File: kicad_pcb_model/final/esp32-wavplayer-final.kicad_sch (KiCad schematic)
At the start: 0 parts

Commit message: Creating schematic
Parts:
- added C1, C3, UC13: 100nF, symbol Device:C
- added C10: C_Polarized_Small_US, Package_SO:SOIC-8_3.9x4.9mm_P1.27mm, symbol Device:C_Polarized_Small_US
- added C11, C7, C8, C9: C, symbol Device:C
- added C2: 10nF, symbol Device:C
- added C4, UC1, UC2, UC3: 1uF, symbol Device:C
- added C5, PC2: 10uF, symbol Device:C
- added C6: C, Display:OLED-128O064D, symbol Device:C
- added DB1: MicroSDDebug, symbol Connector:Conn_01x06_Pin
- added DB2: DisplayDebug, symbol Connector:Conn_01x04_Pin
- added DS1: Wisevision X096-2864KSWPG01-H30, Display:OLED-128O064D, symbol Display_Graphic:OLED-128O064D
- added MSD1: Generic MicroSD, Module:Maple_Mini, symbol Connector:Micro_SD_Card_Det1
- added PC1: 10uF, Package_TO_SOT_SMD:SOT-23-5, symbol Device:C
- added R1, R2, R3, R4: 10k, symbol Device:R
- added R10, R7, R8, R9: 22R, symbol Device:R
- added R11: R, symbol Device:R
- added R5, R6: 5.1K, Package_DIP:DIP-8_W7.62mm, symbol Device:R
- added U1: ESP32-C3, Package_DFN_QFN:QFN-32-1EP_5x5mm_P0.5mm_EP3.45x3.45mm, symbol PCM_Espressif:ESP32-C3
- added U2: ME6211C33M5, Package_TO_SOT_SMD:SOT-23-5, symbol Regulator_Linear:ME6211C33M5
- added USB1: USBC-6Pin, symbol Connector:USB_C_Receptacle_USB2.0_14P
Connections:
- new net: C11.2, DS1.28 (VCC)
- new net: R6.1, USB1.A5 (CC1)
- new net: R10.2, USB1.A6 (D+)
- new net: R7.2, USB1.A7 (D-)
- new net: R5.1, USB1.B5 (CC2)
- new net: R9.2, USB1.B6 (D+)
- new net: R8.2, USB1.B7 (D-)
- new net: DS1.26 (IREF), R11.2
- new net: C8.1, DS1.6 (VBAT)
- new net: C9.1, DS1.12 (BS2), DS1.9 (VDD)
- new net: C6.2, DS1.2 (C2N)
- new net: C10.1, DS1.27 (VCOMH)
- new net: C6.1, DS1.3 (C2P)
- new net: C7.1, DS1.4 (C1P)
- new net: C7.2, DS1.5 (C1N)
- new net +3V3: C1.1, C2.1, C3.1, C4.1, C5.1, DB1.1 (Pin_1), MSD1.4 (VDD), PC2.1, R1.1, R2.1, R3.1, R4.1, U1.11 (VDD3P3_RTC), U1.17 (VDD3P3_CPU), U1.2 (VDD3P3), U1.3 (VDD3P3), U1.31 (VDDA), U1.32 (VDDA), U2.5 (V_{OUT}), UC1.1, UC13.2, UC2.1, UC3.1
- new net Earth: C1.2, C10.2, C11.1, C2.2, C3.2, C4.2, C5.2, C8.2, C9.2, DB1.6 (Pin_6), DS1.1 (GND), DS1.10 (BS0), DS1.11 (BS1), DS1.29 (VLSS), DS1.30 (GND), DS1.8 (VSS), MSD1.6 (VSS), PC1.2, PC2.2, R11.1, R5.2, R6.2, U1.33 (GND), U2.2 (V_{SS}), UC1.2, UC13.1, UC2.2, UC3.2, USB1.A1 (GND), USB1.A12 (GND), USB1.B1 (GND), USB1.B12 (GND)
- new net GPIO18/USB_D+: R10.1, R9.1
- new net GPIO18/USB_D-: U1.25 (GPIO18/USB_D-)
- new net GPIO19/USB_D+: U1.26 (GPIO19/USB_D+)
- new net GPIO19/USB_D-: R7.1, R8.1
- new net GPIO4: DB1.4 (Pin_4), MSD1.5 (CLK), R2.2, U1.9 (MTMS/GPIO4/ADC1_CH4)
- new net GPIO5: DB1.5 (Pin_5), MSD1.7 (DAT0), R1.2, U1.10 (MTDI/GPIO5/ADC2_CH0)
- new net GPIO6: DB1.3 (Pin_3), MSD1.3 (CMD), R3.2, U1.12 (MTCK/GPIO6)
- new net GPIO7: DB1.2 (Pin_2), MSD1.2 (DAT3/CD), R4.2, U1.13 (MTDO/GPIO7)
- new net VBUS: PC1.1, U2.1 (V_{IN}), U2.3 (CE), USB1.A4 (VBUS), USB1.A9 (VBUS), USB1.B4 (VBUS), USB1.B9 (VBUS)
- no-connect marks 0 -> 3
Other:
- note added: "3v3"
- note added: "CS"
- note added: "GND"
- note added: "MISO"
- note added: "MOSI"
- note added: "SCK"

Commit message: editing
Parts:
- removed C10: C_Polarized_Small_US, Package_SO:SOIC-8_3.9x4.9mm_P1.27mm, symbol Device:C_Polarized_Small_US
- added A1: 3.5mmAudioJack, Package_QFP:TQFP-48-1EP_7x7mm_P0.5mm_EP3.5x3.5mm, symbol Connector_Audio:AudioPlug3
- added C10, C12, C19: C, symbol Device:C
- added C13, C14, C16, C18: 0.1uF, symbol Device:C
- added C15, C17: 10uF, symbol Device:C
- added C20, C21: 2.2, symbol Device:C
- added D1: D, symbol Device:D
- added DB3: PCM5102aDebug, Package_SO:TSSOP-20_4.4x6.5mm_P0.65mm, symbol Connector:Conn_01x06_Pin
- added F2, F3: ME6211C33M5, Package_TO_SOT_SMD:SOT-23-5, symbol Regulator_Linear:ME6211C33M5
- added R12, R13: R, symbol Device:R
- added R14: 1k, symbol Device:R
- added U3: PCM5102A, Package_SO:TSSOP-20_4.4x6.5mm_P0.65mm, symbol Audio:PCM5102A
- renumbered U2 to F1
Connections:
- net +3V3: now also DB2.1 (Pin_1), C13.1, C14.1, DB3.6 (Pin_6), F2.1 (V_{IN}), F2.3 (CE), F3.1 (V_{IN}), F3.3 (CE)
- net Earth: now also DB2.2 (Pin_2), DS1.12 (BS2), DS1.13 (~{CS}), DS1.15 (D/~{C}), DS1.16 (R/~{W}), DS1.17 (E/~{RD}), DS1.21 (D3), DS1.22 (D4), DS1.23 (D5), DS1.24 (D6), DS1.25 (D7), A1.S, C10.1, C12.2, C13.2, C14.2, C15.2, C16.2, C17.2, C18.2, D1.1 (K), DB3.1 (Pin_1), DB3.5 (Pin_5), F2.2 (V_{SS}), F3.2 (V_{SS}), U3.10 (DEMP), U3.11 (FLT), U3.12 (SCK), U3.16 (FMT), U3.19 (DGND), U3.9 (AGND); no longer DS1.11 (BS1)
- net SDA: now reaches U1.14 (GPIO8)
- net SDA: now also DB2.4 (Pin_4), DS1.19 (D1), DS1.20 (D2), R12.2
- net SCL: now reaches U1.15 (GPIO9/BOOT)
- net SCL: now also DB2.3 (Pin_3), DS1.18 (D0), R13.2
- net GPIO1: now reaches U1.5 (XTAL_32K_N/ADC1_CH1)
- net GPIO1: now also DB3.2 (Pin_2), U3.13 (BCK)
- net GPIO2: now reaches U1.6 (GPIO2/ADC1_CH2)
- net GPIO2: now also DB3.3 (Pin_3), U3.14 (DIN)
- net GPIO3: now reaches U1.8 (GPIO3/ADC1_CH3)
- net GPIO3: now also DB3.4 (Pin_4), U3.15 (LRCK)
- net VDD: now reaches C9.1, DS1.9 (VDD)
- net VDD: now also DS1.11 (BS1), C12.1, R12.1, R13.1; no longer DS1.12 (BS2)
- net RES#: now reaches DS1.14 (~{RES})
- net at DS1.27 (VCOMH): now also C10.2
- new net: C17.1, C18.1, F3.5 (V_{OUT}), R14.1, U3.8 (AVDD)
- new net: A1.R, U3.7 (OUTR)
- new net: A1.T, U3.6 (OUTL)
- new net: C19.1, U3.3 (CPGND)
- new net: C19.2, C21.2
- new net: C21.1, U3.5 (VNEG)
- new net: C15.1, C16.1, F2.5 (V_{OUT}), U3.17 (XSMT), U3.20 (DVDD)
- new net: D1.2 (A), R14.2
- new net: C20.1, U3.2 (CAPP)
- new net: C20.2, U3.4 (CAPM)
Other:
- moved on the sheet: C3, C4, C5, DB2, U1, UC1, UC13, UC2, UC3

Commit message: Audio hookup
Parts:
- added C22, C24: 0.1uF, symbol Device:C
- added C23: 10uF, symbol Device:C
- added C25, C26: 2.2uF, symbol Device:C
- added R15, R16: 470, symbol Device:R
- C19: value C -> 10uF
- C20, C21: value 2.2 -> 2.2uF
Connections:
- net Earth: now also C19.2, C22.2, C23.1, C24.1, C25.2, C26.2; no longer DB3.1 (Pin_1)
- net GPIO1: now also DB3.3 (Pin_3); no longer DB3.2 (Pin_2)
- net GPIO2: now also DB3.2 (Pin_2); no longer DB3.3 (Pin_3)
- net GPIO3: now also DB3.1 (Pin_1); no longer DB3.4 (Pin_4)
- net at C17.1, C18.1, F3.5 (V_{OUT})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: now also U3.1 (CPVDD)
- net at A1.R: now also C26.1, R15.2; no longer U3.7 (OUTR)
- net at A1.T: now also C25.1, R16.2; no longer U3.6 (OUTL)
- net at C19.1: now also C15.1, C16.1, F2.5 (V_{OUT}), U3.17 (XSMT), U3.20 (DVDD), C22.1; no longer U3.3 (CPGND)
- net at C21.2: now also U3.3 (CPGND); no longer C19.2
- net at U3.18 (LDOO): now also C23.2, C24.2
- new net: R15.1, U3.7 (OUTR)
- new net: R16.1, U3.6 (OUTL)
- no-connect marks 3 -> 4
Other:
- moved on the sheet: A1, C1, C13, C15, C16, C2, C20, C21, D1, DB1, DB3, F2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

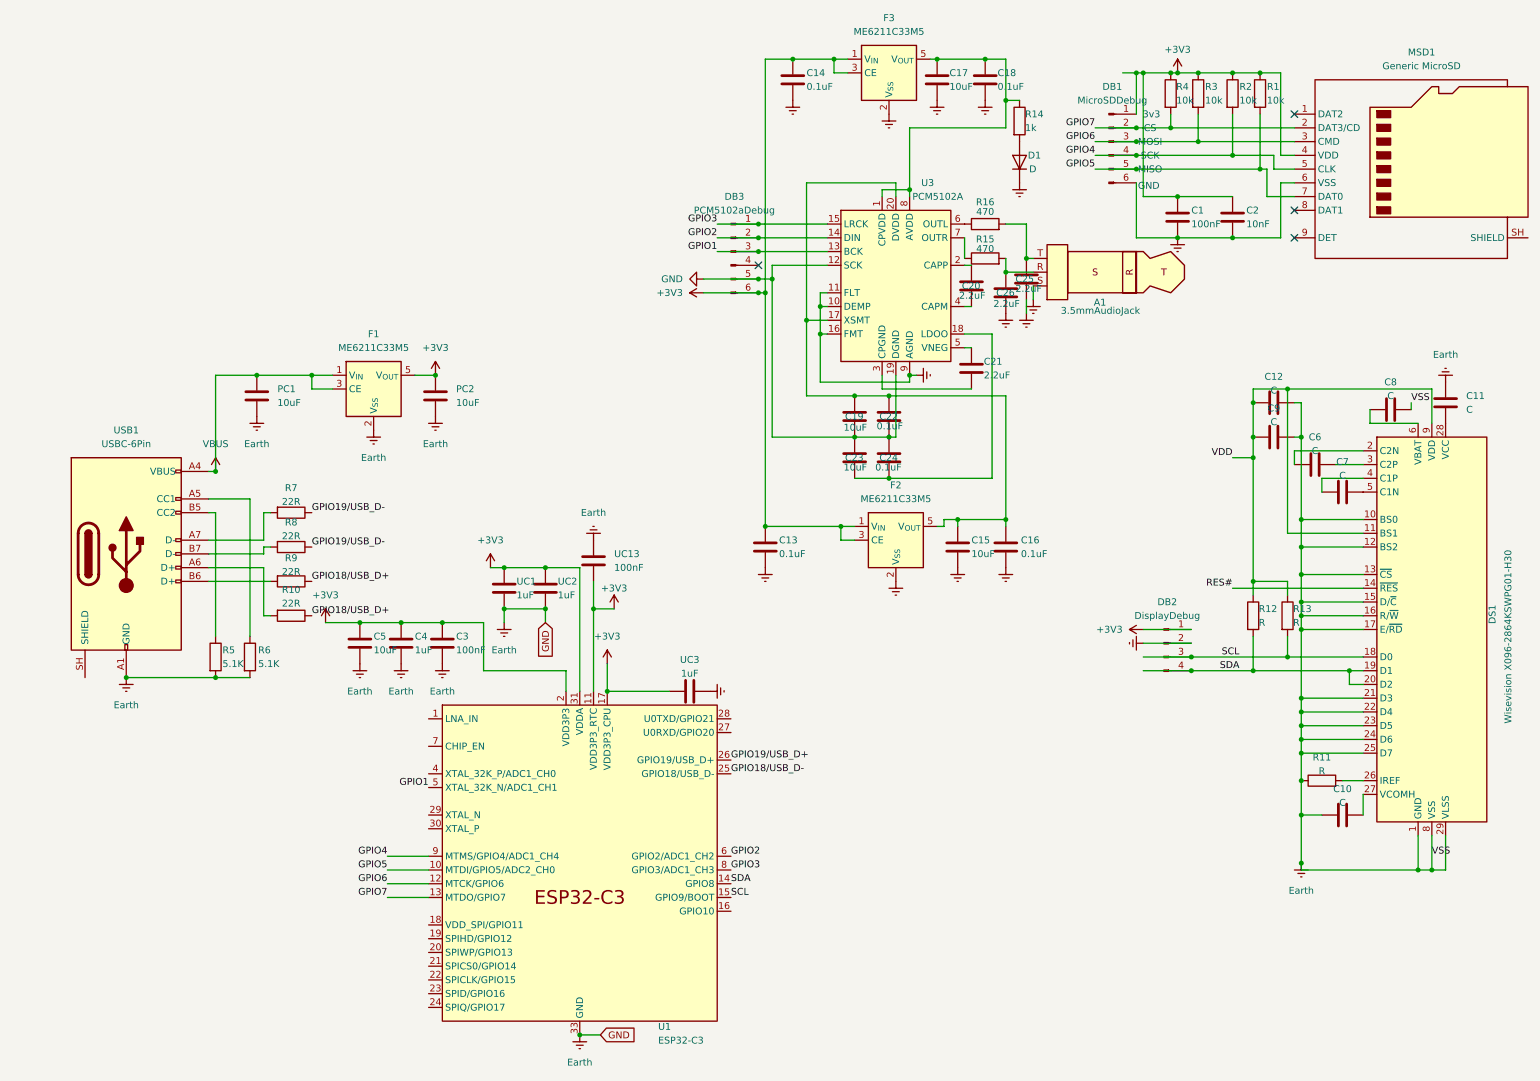
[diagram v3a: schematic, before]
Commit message: Organizing Schematic
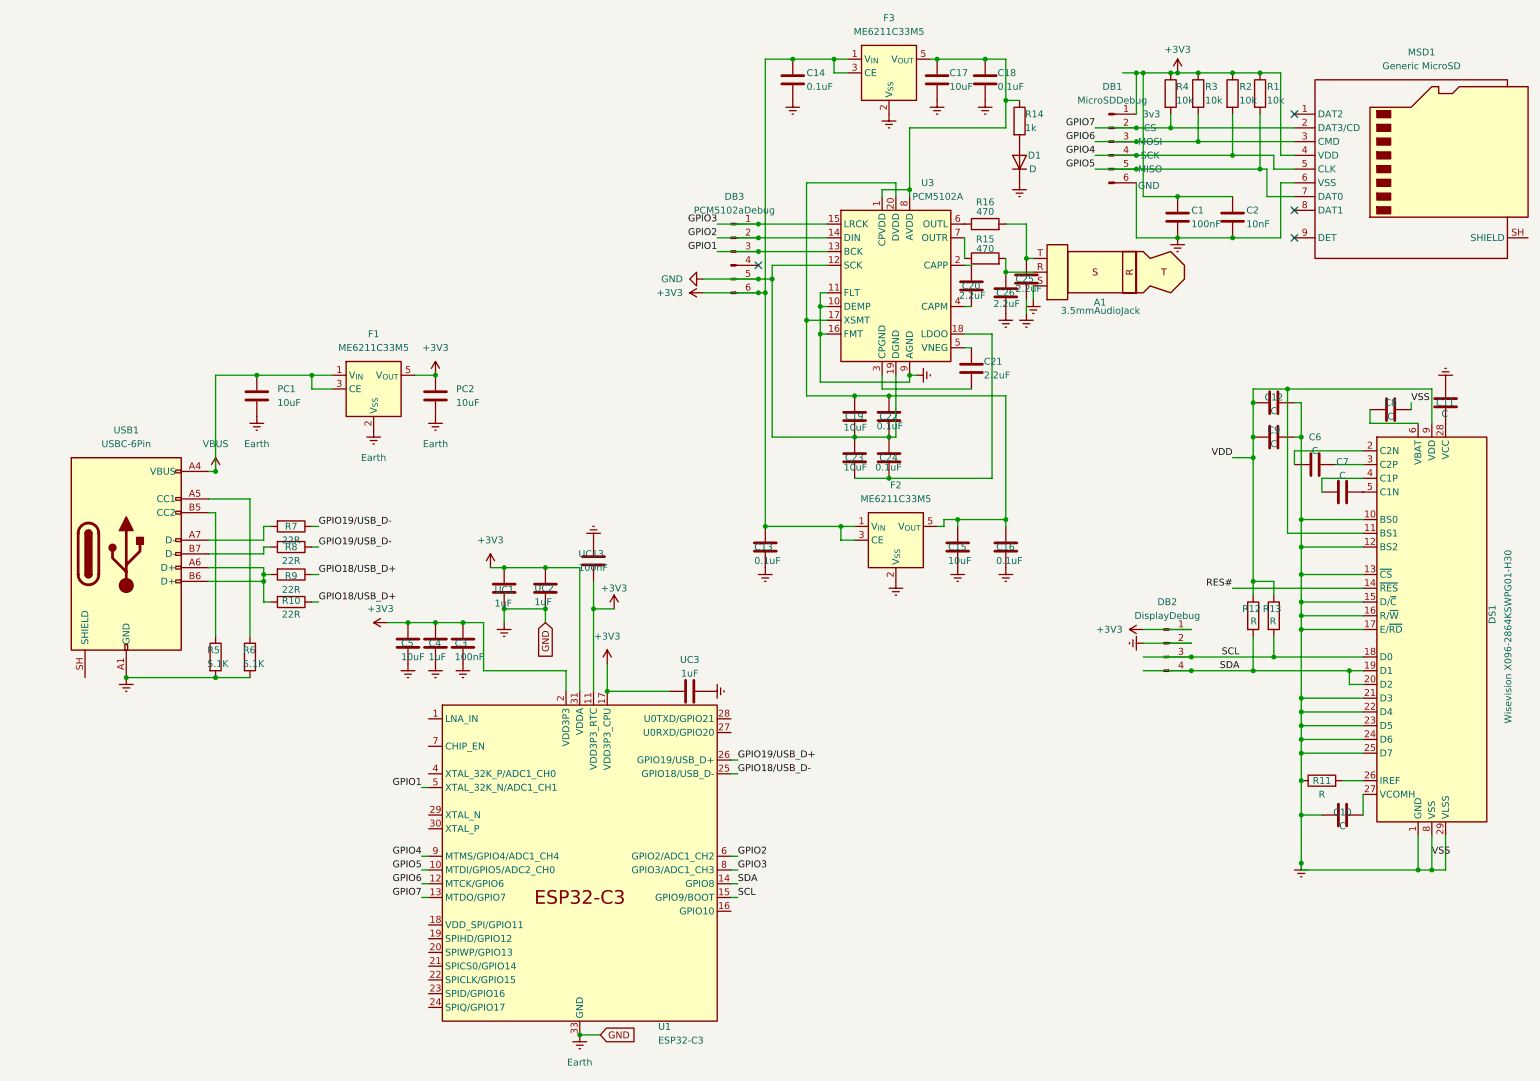
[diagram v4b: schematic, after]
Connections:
- net at R10.2, USB1.A6 (D+): now also R9.2, USB1.B6 (D+)
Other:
- moved on the sheet: C3, C4, C5, R10, R13, R7, R9

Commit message: Added crystal, input, and leds
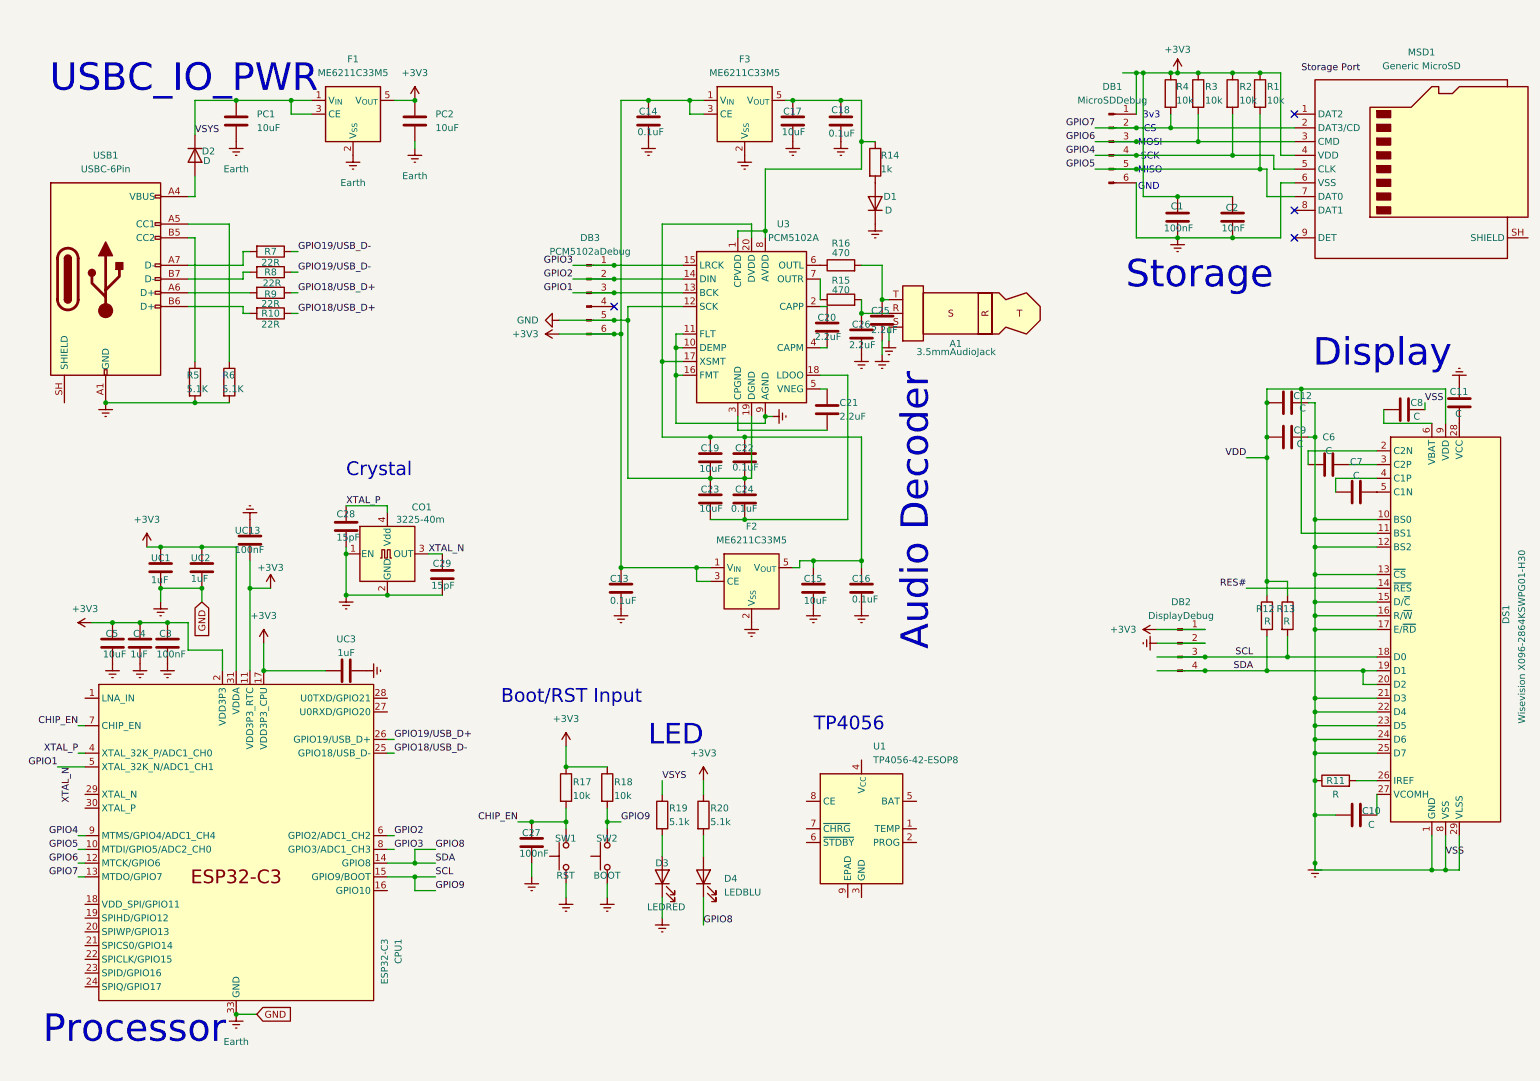
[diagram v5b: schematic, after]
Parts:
- added C27: 100nF, symbol Device:C
- added C28, C29: 15pF, Oscillator:Oscillator_SMD_Abracon_ASE-4Pin_3.2x2.5mm, symbol Device:C
- added CO1: 3225-40m, Oscillator:Oscillator_SMD_Abracon_ASE-4Pin_3.2x2.5mm, symbol Oscillator:ASE-xxxMHz
- added D2: D, symbol Device:D
- added D3: LEDRED, symbol Device:LED
- added D4: LEDBLU, symbol Device:LED
- added R17, R18: 10k, symbol Device:R
- added R19, R20: 5.1k, symbol Device:R
- added SW1: RST, Button_Switch_THT:SW_NKK_GW12LJP, symbol Switch:SW_Push
- added SW2: BOOT, symbol Switch:SW_Push
- added U1: TP4056-42-ESOP8, Package_SO:SOIC-8-1EP_3.9x4.9mm_P1.27mm_EP2.41x3.3mm_ThermalVias, symbol Battery_Management:TP4056-42-ESOP8
- renumbered U1 to CPU1
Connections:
- net +3V3: now also R17.1, R18.1, R20.1
- net Earth: now also C27.2, C28.2, C29.2, CO1.1 (EN), CO1.2 (GND), D3.1 (K), SW1.1, SW2.1
- net GPIO1: now also C29.1, CO1.3 (OUT)
- net at R9.2, USB1.A6 (D+): no longer R10.2, USB1.B6 (D+)
- net XTAL_P: now reaches CPU1.4 (XTAL_32K_P/ADC1_CH0)
- net XTAL_P: now also C28.1, CO1.4 (Vdd)
- net CHIP_EN: now reaches CPU1.7 (CHIP_EN)
- net CHIP_EN: now also C27.1, R17.2, SW1.2
- net SCL renamed GPIO9
- net GPIO9: now also R18.2, SW2.2
- net SDA renamed GPIO8
- net GPIO8: now also D4.1 (K)
- net VBUS: no longer names the net of USB1.A4 (VBUS), USB1.A9 (VBUS), USB1.B4 (VBUS), USB1.B9 (VBUS)
- net VBUS: now also D2.2 (A); no longer F1.1 (V_{IN}), F1.3 (CE), PC1.1
- new net: R10.2, USB1.B6 (D+)
- new net: D3.2 (A), R19.2
- new net: D4.2 (A), R20.2
- new net VSYS: D2.1 (K), F1.1 (V_{IN}), F1.3 (CE), PC1.1, R19.1
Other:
- note added: "Audio Decoder"
- note added: "Boot/RST Input"
- note added: "Crystal"
- note added: "Display"
- note added: "LED"
- note added: "Processor"
- note added: "Storage"
- note added: "TP4056"
- note added: "USBC_IO_PWR"
- moved on the sheet: A1, C10, C11, C12, C13, C14, C15, C16, C17, C18, C19, C20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

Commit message: Added tp4096
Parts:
- added BT1: Battery_Cell, Package_TO_SOT_SMD:SOT-23-5, symbol Device:Battery_Cell
- added C30, C31: 10uF, symbol Device:C
- added D5, D6: LED, Display:OLED-128O064D, symbol Device:LED
- added R21: 0.4, symbol Device:R
- added R22, R23, R24: 1k, symbol Device:R
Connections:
- net Earth: now also U1.1 (TEMP), U1.3 (GND), BT1.2 (-), C30.2, C31.2, R24.2
- net VSYS: now also R21.2
- net at U1.2 (PROG): now also R24.1
- net at U1.4 (V_{CC}): now also U1.8 (CE), C30.1, D5.2 (A), D6.2 (A), R21.1
- net at U1.5 (BAT): now also BT1.1 (+), C31.1
- net at U1.6 (~{STDBY}): now also R22.2
- net at U1.7 (~{CHRG}): now also R23.2
- new net: D5.1 (K), R23.1
- new net: D6.1 (K), R22.1
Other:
- moved on the sheet: A1, C13, C14, C15, C16, C17, C18, C19, C20, C21, C22, C23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
